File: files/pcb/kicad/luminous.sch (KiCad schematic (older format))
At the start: 2 parts

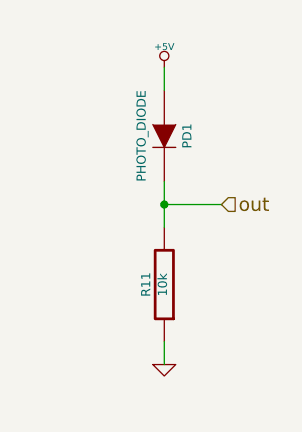
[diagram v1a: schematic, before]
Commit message: 設計見直し
部品見直し
USB・DCジャック自動切り替え
マイコンを下段のボードに移動
ニキシー管駆動電源を上段ボードに移動
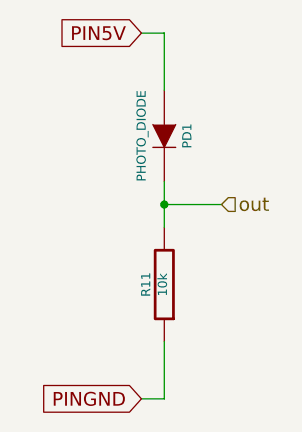
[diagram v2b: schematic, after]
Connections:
- net +5V renamed PIN5V
- net GND renamed PINGND
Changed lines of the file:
@@
 $Descr A4 11693 8268
 encoding utf-8
-Sheet 4 11
+Sheet 4 8
 Title ""
-Date "31 aug 2014"
+Date "1 sep 2014"
 Rev ""
 Comp ""
@@
 	-1   0    0    1
 $EndComp
-$Comp
-L GND #PWR021
-U 1 1 53F8E33E
-P 5700 4450
-F 0 "#PWR021" H 5700 4450 30  0001 C CNN
-F 1 "GND" H 5700 4380 30  0001 C CNN
-F 2 "" H 5700 4450 60  0000 C CNN
-F 3 "" H 5700 4450 60  0000 C CNN
-	1    5700 4450
-	1    0    0    -1
-$EndComp
-$Comp
-L +5V #PWR022
-U 1 1 53F8E34D
-P 5700 3150
-F 0 "#PWR022" H 5700 3240 20  0001 C CNN
-F 1 "+5V" H 5700 3240 30  0000 C CNN
-F 2 "" H 5700 3150 60  0000 C CNN
-F 3 "" H 5700 3150 60  0000 C CNN
-	1    5700 3150
-	1    0    0    -1
-$EndComp
 Wire Wire Line
-	5700 3250 5700 3150
+	5700 3000 5700 3250
 Wire Wire Line
 	5700 3650 5700 3850
 Wire Wire Line
-	5700 4350 5700 4450
+	5700 4350 5700 4600
 Wire Wire Line
 	5950 3750 5700 3750
 Connection ~ 5700 3750
+Text GLabel 5600 4600 0    60   Input ~ 0
+PINGND
+Text GLabel 5600 3000 0    60   Input ~ 0
+PIN5V
+Wire Wire Line
+	5600 3000 5700 3000
+Wire Wire Line
+	5700 4600 5600 4600
 $EndSCHEMATC
